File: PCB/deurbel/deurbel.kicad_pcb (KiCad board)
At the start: 2 copper layers, 80.1 x 65 mm, 25 parts, among them J1 Mute, J2 Doorbell, J3 Test_Doorbell, J4 Powerline, J5 Gong, K2 SRD-05VDC-SL-C, Q1 2N7000, Q2 BC338, U2 LM7805_TO220

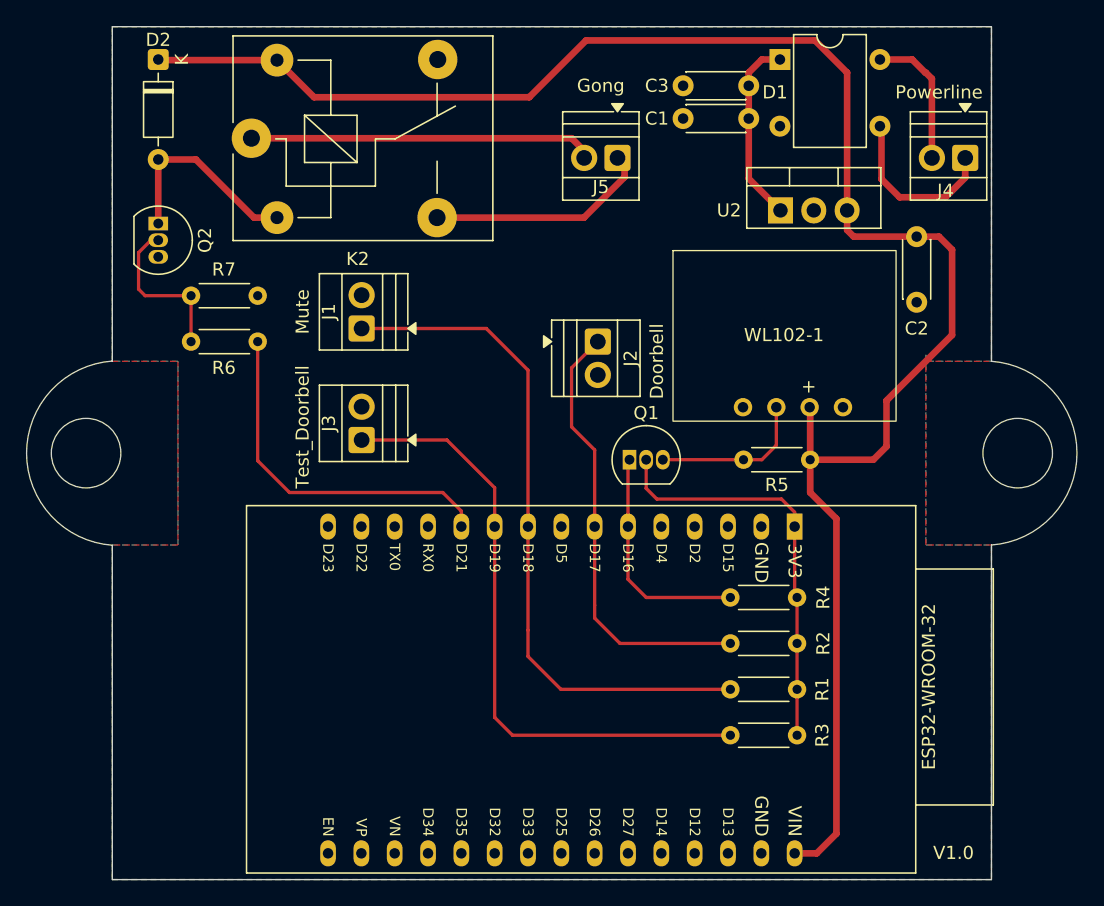
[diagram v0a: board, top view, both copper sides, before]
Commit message: Client config is now done once and removed scanning from connection task
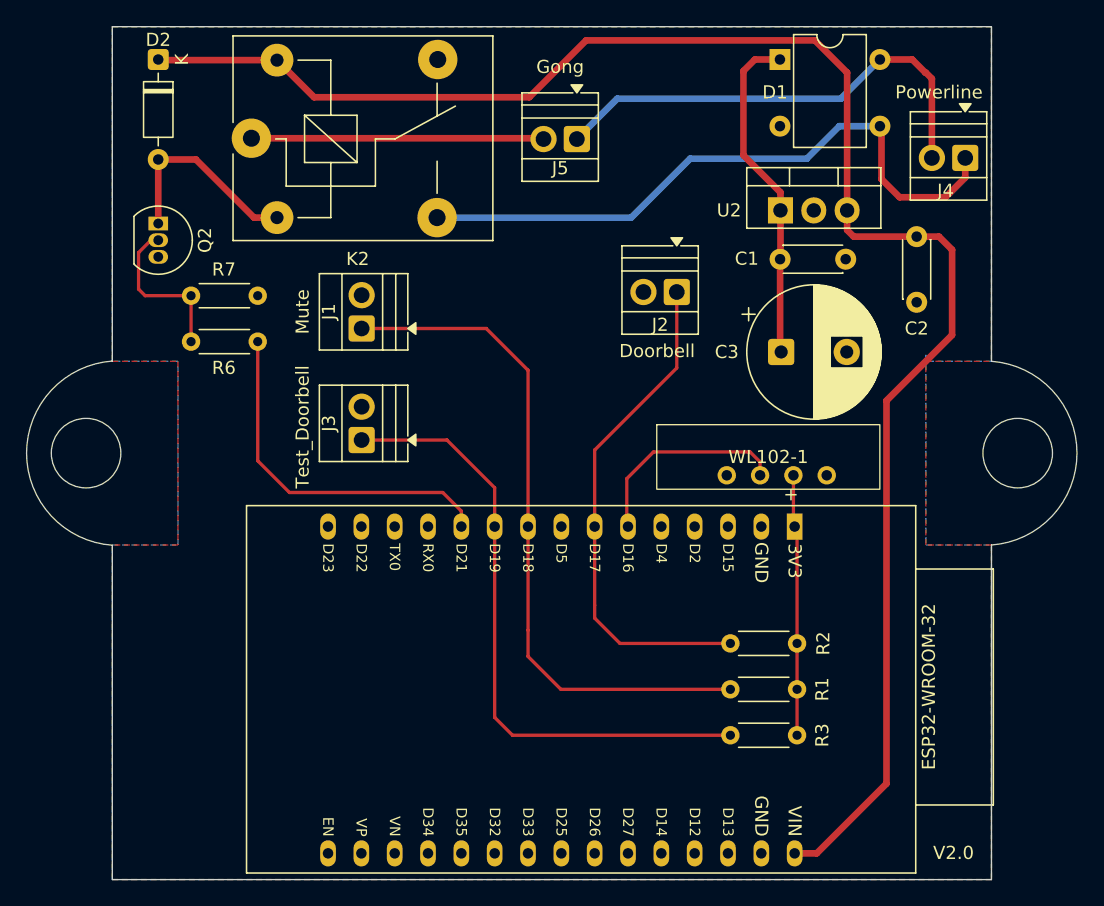
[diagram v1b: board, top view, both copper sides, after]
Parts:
- removed Q1: 2N7000, Package_TO_SOT_THT:TO-92_Inline
- removed R4, R5: 10k, Resistor_THT:R_Axial_DIN0204_L3.6mm_D1.6mm_P5.08mm_Horizontal
- C2: value 10nF -> 100nF
- C3: footprint Capacitor_THT:C_Disc_D4.3mm_W1.9mm_P5.00mm -> Capacitor_THT:CP_Radial_D10.0mm_P5.00mm
- moved C3 20.4 mm to (215.5, 97.8), turned to 0 degrees
- moved WL102-1 13.3 mm to (206.0, 103.3)
- moved C1 11.0 mm to (215.4, 90.7), turned to 0 degrees
- moved J2 7.11 mm to (207.5, 93.2), turned to 180 degrees
- moved J5 3.41 mm to (199.9, 81.6)
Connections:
- C2 pad 1: 5V -> +5V
- D1 pad 3: Net-(J4-Pin_1) -> PWR1
- D1 pad 4: Net-(J4-Pin_2) -> PWR2
- D2 pad 1: 5V -> +5V
- ESP32-WROOM-32 pad 1: 3V3 -> +3.3V
- ESP32-WROOM-32 pad 16: 5V -> +5V
- J4 pad 1: Net-(J4-Pin_1) -> PWR1
- J4 pad 2: Net-(J4-Pin_2) -> PWR2
- J5 pad 1: Net-(J5-Pin_1) -> PWR2
- K2 pad 3: Net-(J5-Pin_1) -> PWR1
- K2 pad 5: 5V -> +5V
- R1 pad 1: 3V3 -> +3.3V
- R2 pad 1: 3V3 -> +3.3V
- R3 pad 1: 3V3 -> +3.3V
- U2 pad 3: 5V -> +5V
- WL102-1 pad 2: 5V -> +3.3V
- WL102-1 pad 3: Net-(Q1-D) -> D16
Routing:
- net 5V: track 137.6 -> 0.00 mm
- net +5V: track 0.00 -> 129.1 mm
- net PWR1: track 0.00 -> 49.8 mm
- net PWR2: track 0.00 -> 35.1 mm
- net 3V3: track 31.3 -> 0.00 mm
- net +3.3V: track 0.00 -> 20.3 mm
- net Net-(J5-Pin_1): track 17.0 -> 0.00 mm
- net Net-(J4-Pin_1): track 13.1 -> 0.00 mm
- net Net-(Q1-D): track 12.0 -> 0.00 mm
- net Net-(D1-+): track 14.4 -> 25.9 mm
- net Net-(J4-Pin_2): track 9.48 -> 0.00 mm
- net Net-(ESP32-WROOM-32-D17): track 33.6 -> 38.6 mm
- net Net-(J5-Pin_2): track 26.5 -> 22.3 mm
- net D16: track 17.5 -> 15.8 mm
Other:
- board text added: "V2.0"
- board text removed: "V1.0"
